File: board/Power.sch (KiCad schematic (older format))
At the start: 15 parts, among them U3 L78L05_TO92

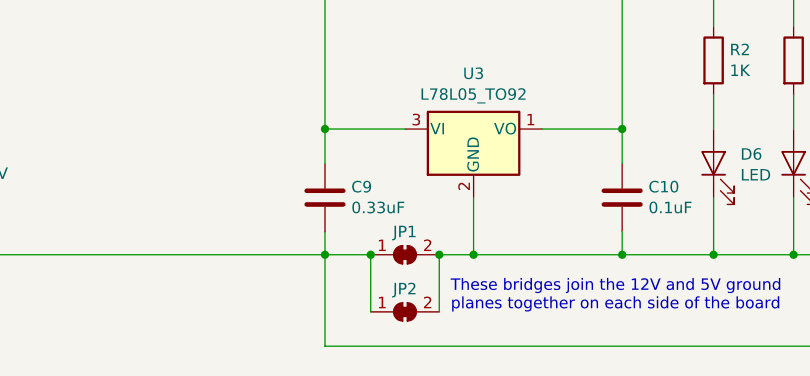
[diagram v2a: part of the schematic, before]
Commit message: Add/correct a bunch of part numbers
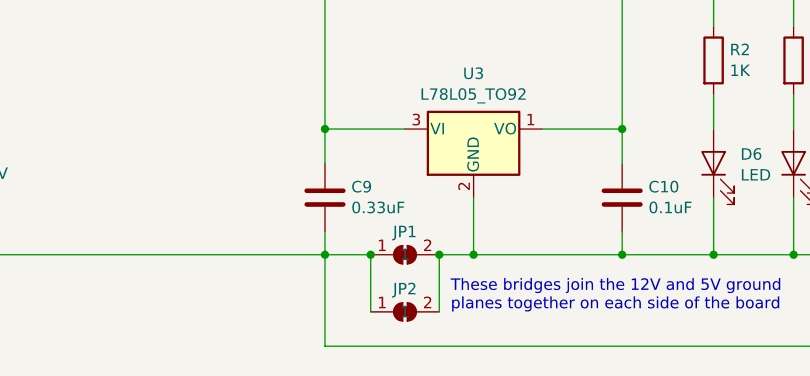
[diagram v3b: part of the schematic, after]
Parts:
- C10: Src1 (none) -> Mouser; Src1 Part (none) -> 810-FG18X7R1H104KNT6; Src1 URL (none) -> https://www.mouser.com/ProductDetail/810-FG18X7R1H104KNT6; mfr (none) -> TDK; mpn (none) -> FG18X7R1H104KNT06
- C11: Src1 (none) -> Mouser; Src1 Part (none) -> 810-FG18X7R1E105KRT0; Src1 URL (none) -> https://www.mouser.com/ProductDetail/810-FG18X7R1E105KRT0; mfr (none) -> TDK; mpn (none) -> FG18X7R1E105KRT00
- C12: Src1 (none) -> Mouser; Src1 Part (none) -> 647-UPW1E471MPD; Src1 URL (none) -> https://www.mouser.com/ProductDetail/647-UPW1E471MPD; mfr (none) -> Nichicon; mpn (none) -> UPW1E471MPD
- C9: Src1 (none) -> Mouser; Src1 Part (none) -> 810-FG18X7R1H334KRT0; Src1 URL (none) -> https://www.mouser.com/ProductDetail/810-FG18X7R1H334KRT0; mfr (none) -> TDK; mpn (none) -> FG18X7R1H334KRT00
- D5: Src1 (none) -> Mouser; Src1 Part (none) -> 625-1.5KE15CA-E3; Src1 URL (none) -> https://www.mouser.com/ProductDetail/625-1.5KE15CA-E3; mpn (none) -> 1.5KE15CA-E3/54; part# 1.5KE15CA-E3/54 -> (none)
- JP1, JP2: DNP (none) -> 1
- PS1: Src1 (none) -> Mouser; Src1 Part (none) -> 490-PSK-S20C-12; Src1 URL (none) -> https://www.mouser.com/ProductDetail/490-PSK-S20C-12; mfr (none) -> CUI; mpn (none) -> PSK-S20C-12
- RV1: Src1 (none) -> Mouser; Src1 Part (none) -> 594-2381-595-52316; Src1 URL (none) -> https://www.mouser.com/ProductDetail/594-2381-595-52316; mpn (none) -> VDRS14T230BSE; part# VDRS14T230BSE -> (none)
- RV2: Src1 (none) -> Mouser; Src1 Part (none) -> 594-2381-595-52316; Src1 URL (none) -> https://www.mouser.com/ProductDetail/594-2381-595-52316; mfr (none) -> Vishay; mpn (none) -> VDRS14T230BSE; part# VDRS14T230BSE -> (none)
- U3: Src1 (none) -> Mouser; Src1 Part (none) -> 511-L78L05ABZ-TR; Src1 URL (none) -> https://www.mouser.com/ProductDetail/511-L78L05ABZ-TR; mfr (none) -> ST; mpn (none) -> L78L05ABZ-TR
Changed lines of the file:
@@
 F 2 "Package_TO_SOT_THT:TO-92L" H 7900 3475 50  0001 C CIN
 F 3 "http://www.st.com/content/ccc/resource/technical/document/datasheet/15/55/e5/aa/23/5b/43/fd/CD00000446.pdf/files/CD00000446.pdf/jcr:content/translations/en.CD00000446.pdf" H 7900 3200 50  0001 C CNN
+F 4 "ST" H 7900 3250 50  0001 C CNN "mfr"
+F 5 "L78L05ABZ-TR" H 7900 3250 50  0001 C CNN "mpn"
+F 6 "Mouser" H 7900 3250 50  0001 C CNN "Src1"
+F 7 "511-L78L05ABZ-TR" H 7900 3250 50  0001 C CNN "Src1 Part"
+F 8 "https://www.mouser.com/ProductDetail/511-L78L05ABZ-TR" H 7900 3250 50  0001 C CNN "Src1 URL"
 	1    7900 3250
 	1    0    0    -1
@@
 F 2 "Capacitor_THT:C_Disc_D5.0mm_W2.5mm_P2.50mm" H 7288 3400 50  0001 C CNN
 F 3 "~" H 7250 3550 50  0001 C CNN
+F 4 "TDK" H 7250 3550 50  0001 C CNN "mfr"
+F 5 "FG18X7R1H334KRT00" H 7250 3550 50  0001 C CNN "mpn"
+F 6 "Mouser" H 7250 3550 50  0001 C CNN "Src1"
+F 7 "810-FG18X7R1H334KRT0" H 7250 3550 50  0001 C CNN "Src1 Part"
+F 8 "https://www.mouser.com/ProductDetail/810-FG18X7R1H334KRT0" H 7250 3550 50  0001 C CNN "Src1 URL"
 	1    7250 3550
 	1    0    0    -1
@@
 F 2 "Capacitor_THT:C_Disc_D5.0mm_W2.5mm_P2.50mm" H 8588 3400 50  0001 C CNN
 F 3 "~" H 8550 3550 50  0001 C CNN
+F 4 "TDK" H 8550 3550 50  0001 C CNN "mfr"
+F 5 "FG18X7R1H104KNT06" H 8550 3550 50  0001 C CNN "mpn"
+F 6 "Mouser" H 8550 3550 50  0001 C CNN "Src1"
+F 7 "810-FG18X7R1H104KNT6" H 8550 3550 50  0001 C CNN "Src1 Part"
+F 8 "https://www.mouser.com/ProductDetail/810-FG18X7R1H104KNT6" H 8550 3550 50  0001 C CNN "Src1 URL"
 	1    8550 3550
 	1    0    0    -1
@@
 F 2 "Chris_Power:ACDC-Conv_CUI-PSK-S20C" H 3650 3050 50  0001 C CNN
 F 3 "https://www.cui.com/product/resource/psk-s20c.pdf" H 4050 3000 50  0001 C CNN
+F 4 "CUI" H 3650 3350 50  0001 C CNN "mfr"
+F 5 "PSK-S20C-12" H 3650 3350 50  0001 C CNN "mpn"
+F 6 "Mouser" H 3650 3350 50  0001 C CNN "Src1"
+F 7 "490-PSK-S20C-12" H 3650 3350 50  0001 C CNN "Src1 Part"
+F 8 "https://www.mouser.com/ProductDetail/490-PSK-S20C-12" H 3650 3350 50  0001 C CNN "Src1 URL"
 	1    3650 3350
 	1    0    0    -1
@@
 F 2 "Capacitor_THT:C_Disc_D5.0mm_W2.5mm_P2.50mm" H 4338 3250 50  0001 C CNN
 F 3 "~" H 4300 3400 50  0001 C CNN
+F 4 "TDK" H 4300 3400 50  0001 C CNN "mfr"
+F 5 "FG18X7R1E105KRT00" H 4300 3400 50  0001 C CNN "mpn"
+F 6 "Mouser" H 4300 3400 50  0001 C CNN "Src1"
+F 7 "810-FG18X7R1E105KRT0" H 4300 3400 50  0001 C CNN "Src1 Part"
+F 8 "https://www.mouser.com/ProductDetail/810-FG18X7R1E105KRT0" H 4300 3400 50  0001 C CNN "Src1 URL"
 	1    4300 3400
 	1    0    0    -1
@@
 F 1 "470uF/25V" H 5018 3355 50  0000 L CNN
 F 2 "Capacitor_THT:CP_Radial_D10.0mm_P2.50mm_P5.00mm" H 4938 3250 50  0001 C CNN
-F 3 "~" H 4900 3400 50  0001 C CNN
+F 3 "https://www.mouser.com/datasheet/2/293/e-upw-1219485.pdf" H 4900 3400 50  0001 C CNN
+F 4 "Nichicon" H 4900 3400 50  0001 C CNN "mfr"
+F 5 "UPW1E471MPD" H 4900 3400 50  0001 C CNN "mpn"
+F 6 "Mouser" H 4900 3400 50  0001 C CNN "Src1"
+F 7 "647-UPW1E471MPD" H 4900 3400 50  0001 C CNN "Src1 Part"
+F 8 "https://www.mouser.com/ProductDetail/647-UPW1E471MPD" H 4900 3400 50  0001 C CNN "Src1 URL"
 	1    4900 3400
 	1    0    0    -1
@@
 F 1 "360V" H 2353 3605 50  0000 L CNN
 F 2 "Varistors:RV_Disc_D15.5_W7.2_P7.5" V 2180 3650 50  0001 C CNN
-F 3 "~" H 2250 3650 50  0001 C CNN
+F 3 "https://www.mouser.com/datasheet/2/427/vdrs-101657.pdf" H 2250 3650 50  0001 C CNN
 F 4 "Vishay" H 2250 3650 50  0001 C CNN "mfr"
-F 5 "VDRS14T230BSE" H 2250 3650 50  0001 C CNN "part#"
+F 5 "VDRS14T230BSE" H 2250 3650 50  0001 C CNN "mpn"
+F 6 "Mouser" H 2250 3650 50  0001 C CNN "Src1"
+F 7 "594-2381-595-52316" H 2250 3650 50  0001 C CNN "Src1 Part"
+F 8 "https://www.mouser.com/ProductDetail/594-2381-595-52316" H 2250 3650 50  0001 C CNN "Src1 URL"
 	1    2250 3650
 	1    0    0    -1
@@
 F 1 "360V" H 2903 3605 50  0000 L CNN
 F 2 "Varistors:RV_Disc_D15.5_W7.2_P7.5" V 2730 3650 50  0001 C CNN
-F 3 "~" H 2800 3650 50  0001 C CNN
-F 4 "VDRS14T230BSE" H 2800 3650 50  0001 C CNN "part#"
+F 3 "https://www.mouser.com/datasheet/2/427/vdrs-101657.pdf" H 2800 3650 50  0001 C CNN
+F 4 "Vishay" H 2800 3650 50  0001 C CNN "mfr"
+F 5 "VDRS14T230BSE" H 2800 3650 50  0001 C CNN "mpn"
+F 6 "Mouser" H 2800 3650 50  0001 C CNN "Src1"
+F 7 "594-2381-595-52316" H 2800 3650 50  0001 C CNN "Src1 Part"
+F 8 "https://www.mouser.com/ProductDetail/594-2381-595-52316" H 2800 3650 50  0001 C CNN "Src1 URL"
 	1    2800 3650
 	1    0    0    -1
@@
 F 3 "https://www.mouser.com/datasheet/2/427/15ke-240293.pdf" H 5650 3400 50  0001 C CNN
 F 4 "Vishay" H 5650 3400 50  0001 C CNN "mfr"
-F 5 "1.5KE15CA-E3/54" H 5650 3400 50  0001 C CNN "part#"
+F 5 "1.5KE15CA-E3/54" H 5650 3400 50  0001 C CNN "mpn"
+F 6 "Mouser" H 5650 3400 50  0001 C CNN "Src1"
+F 7 "625-1.5KE15CA-E3" H 5650 3400 50  0001 C CNN "Src1 Part"
+F 8 "https://www.mouser.com/ProductDetail/625-1.5KE15CA-E3" H 5650 3400 50  0001 C CNN "Src1 URL"
 	1    5650 3400
 	0    1    1    0
@@
 F 2 "Jumper:SolderJumper-2_P1.3mm_Bridged2Bar_RoundedPad1.0x1.5mm" H 7600 3800 50  0001 C CNN
 F 3 "~" H 7600 3800 50  0001 C CNN
+F 4 "1" H 7600 3800 50  0000 C CNN "DNP"
 	1    7600 3800
 	1    0    0    -1
@@
 F 2 "Jumper:SolderJumper-2_P1.3mm_Bridged2Bar_RoundedPad1.0x1.5mm" H 7600 4050 50  0001 C CNN
 F 3 "~" H 7600 4050 50  0001 C CNN
+F 4 "1" H 7600 4050 50  0000 C CNN "DNP"
 	1    7600 4050
 	1    0    0    -1

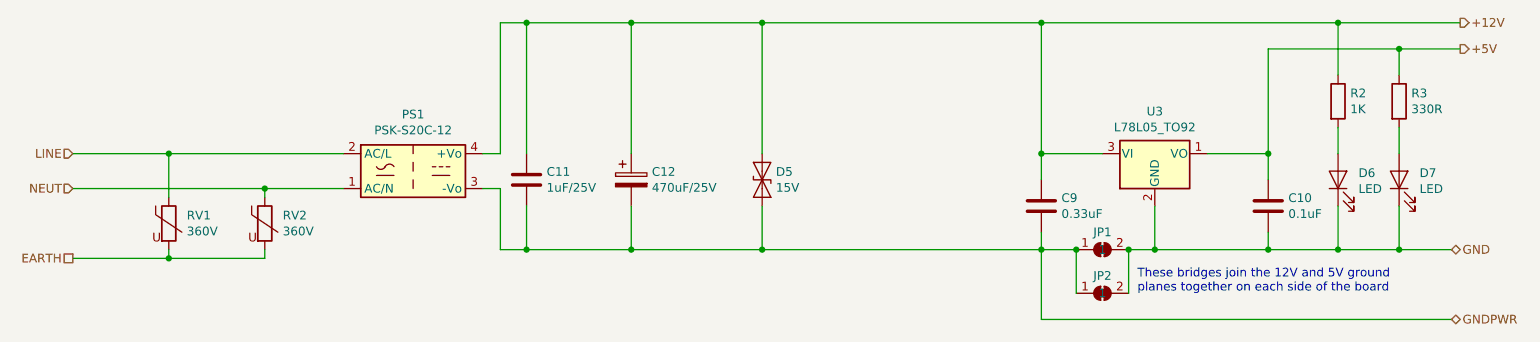
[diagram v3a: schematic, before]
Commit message: Layout adjustments to make room
* Move the relays and diodes left to give a little more room to the
  power connectors; adjust ground planes to suit, etc.
* Larger footprint for TVS diode; related adjustments.
* Other minor adjustments to layout.
* Add board-only preview.
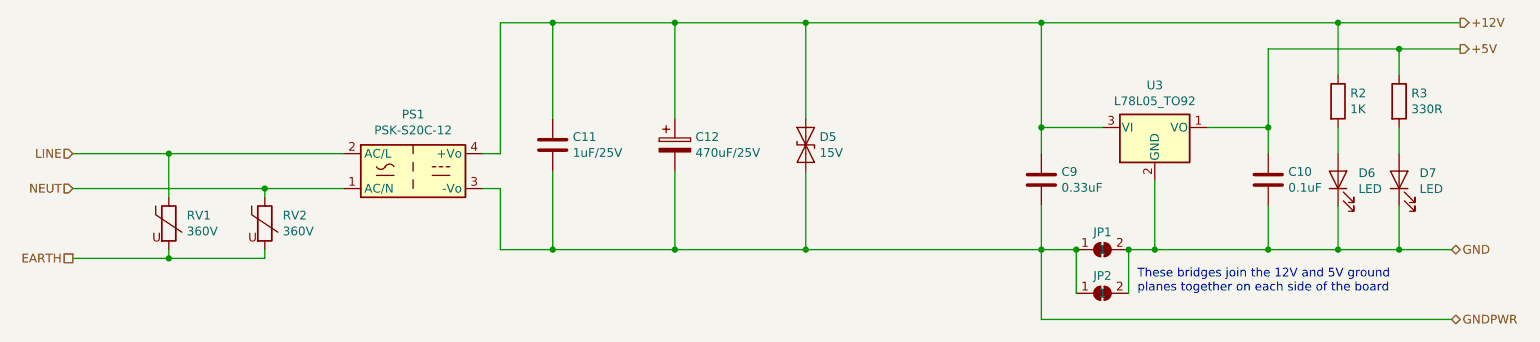
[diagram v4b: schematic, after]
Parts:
- D5: footprint Diode_THT:D_DO-41_SOD81_P10.16mm_Horizontal -> Diodes_THT:D_DO-41_SOD81_P12.70mm_Horizontal
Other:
- moved on the sheet: C10, C11, C12, C9, D5, U3

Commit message: First pass at input protection for buttons
* Schottky diodes & capacitors to limit and smooth the inputs.
* Relies on the WPU of the MCU to provide a charge for the C (possibly
  a bad idea, will see).
* Had to move a bunch of stuff to make room and make sure the ground paths
  were sensible.
* Update all the disc capacitors to the Kicad 5 footprint.
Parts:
- C10, C11, C9: footprint Capacitor_THT:C_Disc_D5.0mm_W2.5mm_P2.50mm -> Capacitors_THT:C_Disc_D5.0mm_W2.5mm_P2.50mm
- D6, D7: footprint LED_THT:LED_D5.0mm -> LEDs:LED_D3.0mm
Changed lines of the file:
@@
 F 0 "C9" H 7365 3446 50  0000 L CNN
 F 1 "0.33uF" H 7365 3355 50  0000 L CNN
-F 2 "Capacitor_THT:C_Disc_D5.0mm_W2.5mm_P2.50mm" H 7288 3250 50  0001 C CNN
+F 2 "Capacitors_THT:C_Disc_D5.0mm_W2.5mm_P2.50mm" H 7288 3250 50  0001 C CNN
 F 3 "~" H 7250 3400 50  0001 C CNN
 F 4 "TDK" H 7250 3400 50  0001 C CNN "mfr"
@@
 F 0 "C10" H 8665 3446 50  0000 L CNN
 F 1 "0.1uF" H 8665 3355 50  0000 L CNN
-F 2 "Capacitor_THT:C_Disc_D5.0mm_W2.5mm_P2.50mm" H 8588 3250 50  0001 C CNN
+F 2 "Capacitors_THT:C_Disc_D5.0mm_W2.5mm_P2.50mm" H 8588 3250 50  0001 C CNN
 F 3 "~" H 8550 3400 50  0001 C CNN
 F 4 "TDK" H 8550 3400 50  0001 C CNN "mfr"
@@
 F 0 "C11" H 4565 3246 50  0000 L CNN
 F 1 "1uF/25V" H 4565 3155 50  0000 L CNN
-F 2 "Capacitor_THT:C_Disc_D5.0mm_W2.5mm_P2.50mm" H 4488 3050 50  0001 C CNN
+F 2 "Capacitors_THT:C_Disc_D5.0mm_W2.5mm_P2.50mm" H 4488 3050 50  0001 C CNN
 F 3 "~" H 4450 3200 50  0001 C CNN
 F 4 "TDK" H 4450 3200 50  0001 C CNN "mfr"
@@
 F 0 "D6" V 8989 3283 50  0000 R CNN
 F 1 "LED" V 8898 3283 50  0000 R CNN
-F 2 "LED_THT:LED_D5.0mm" H 8950 3400 50  0001 C CNN
+F 2 "LEDs:LED_D3.0mm" H 8950 3400 50  0001 C CNN
 F 3 "~" H 8950 3400 50  0001 C CNN
 	1    8950 3400
@@
 F 0 "D7" V 9339 3283 50  0000 R CNN
 F 1 "LED" V 9248 3283 50  0000 R CNN
-F 2 "LED_THT:LED_D5.0mm" H 9300 3400 50  0001 C CNN
+F 2 "LEDs:LED_D3.0mm" H 9300 3400 50  0001 C CNN
 F 3 "~" H 9300 3400 50  0001 C CNN
 	1    9300 3400
